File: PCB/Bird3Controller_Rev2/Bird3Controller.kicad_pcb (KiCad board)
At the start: 2 copper layers, 43 x 108 mm, 52 parts, among them IC1 M24C08-RMN6TP, J1 Bird 3 24-pin Connector, J2 TXW154028S0 Connector, J3 87832-2220, Q1 2N7002A, SW1 SW_Boot, SW2 SW_Reset, U1 ESP32-S3-WROOM-1, U3 SN65HVD231, U4 LMR36520ADDAR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

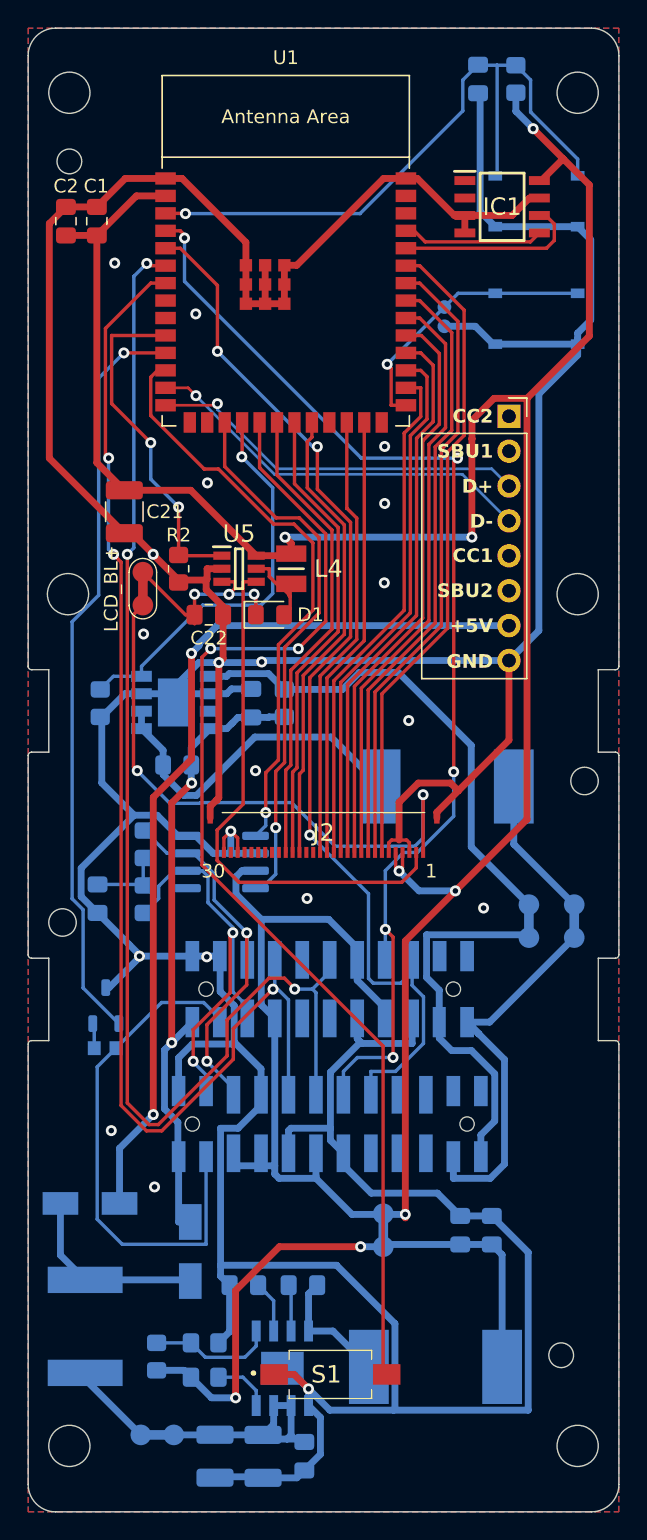
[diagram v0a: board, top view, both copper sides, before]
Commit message: Add more ground-plane vias
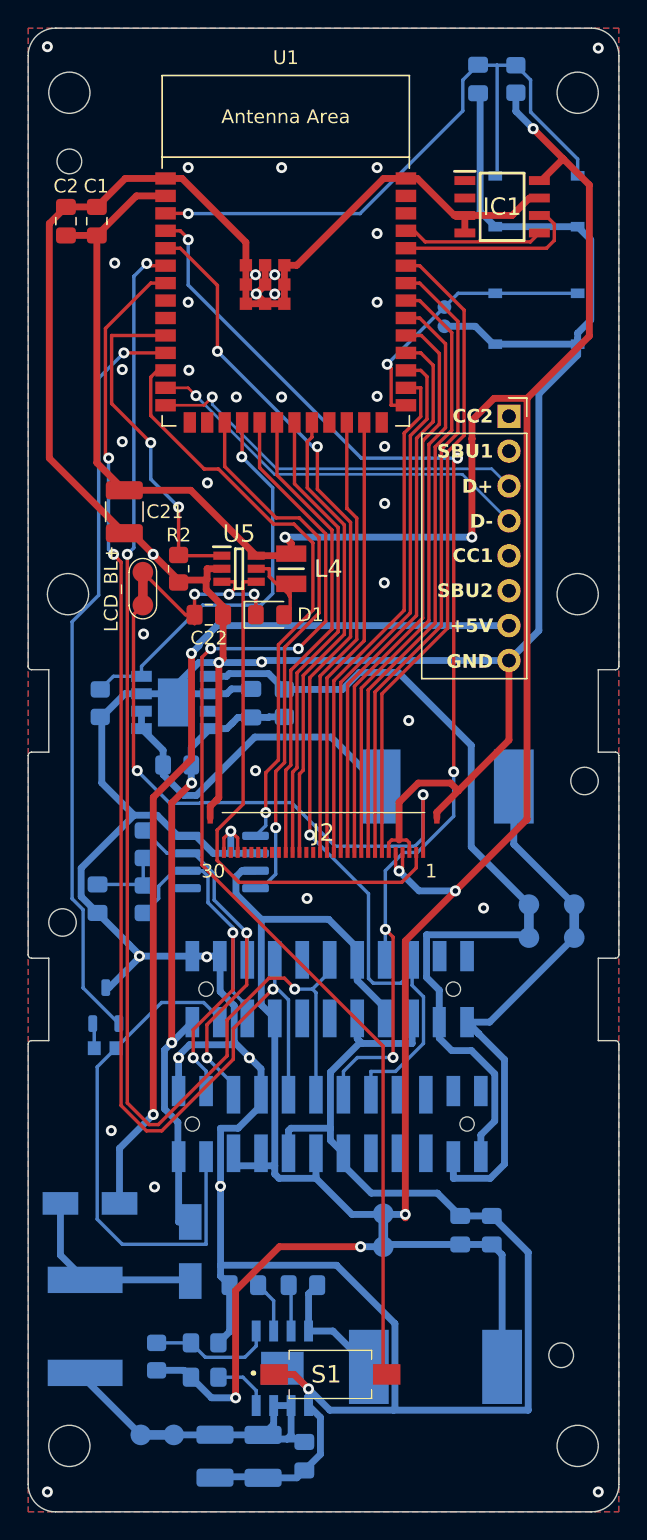
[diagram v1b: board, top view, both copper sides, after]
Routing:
- net GND: track 424.6 -> 425.3 mm, vias 20 -> 42

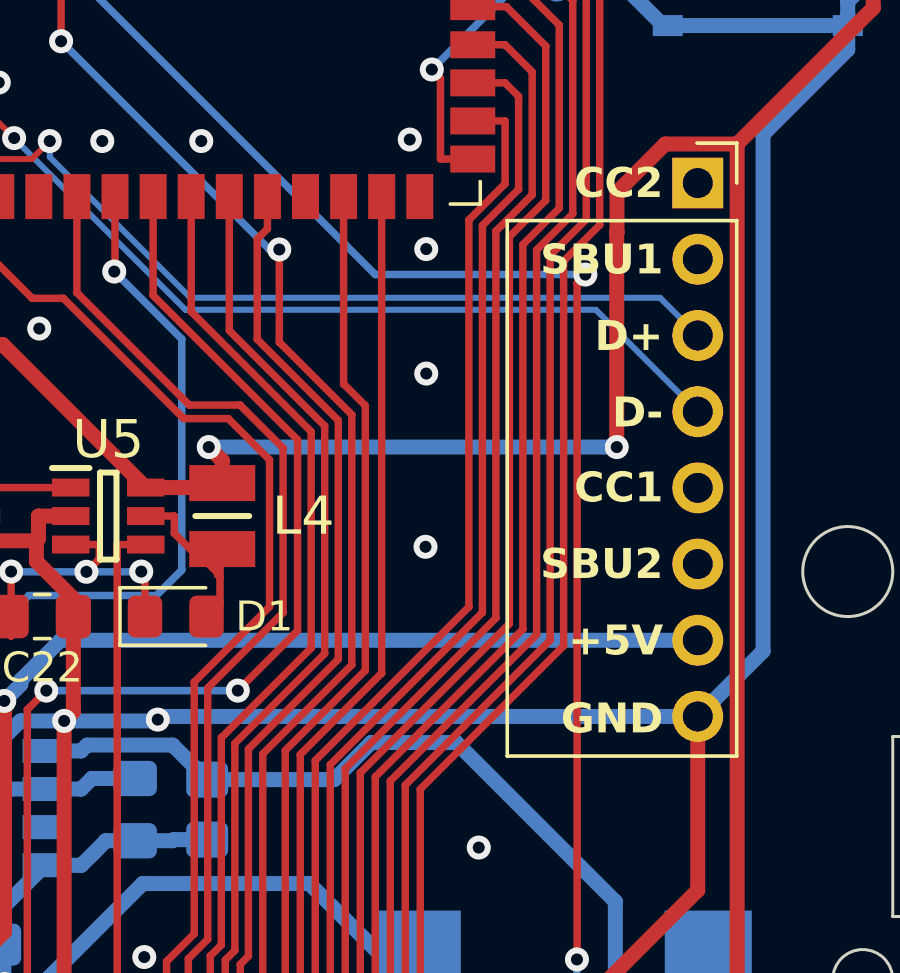
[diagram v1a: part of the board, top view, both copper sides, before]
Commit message: Push LCD data traces around and add more ground plane vias
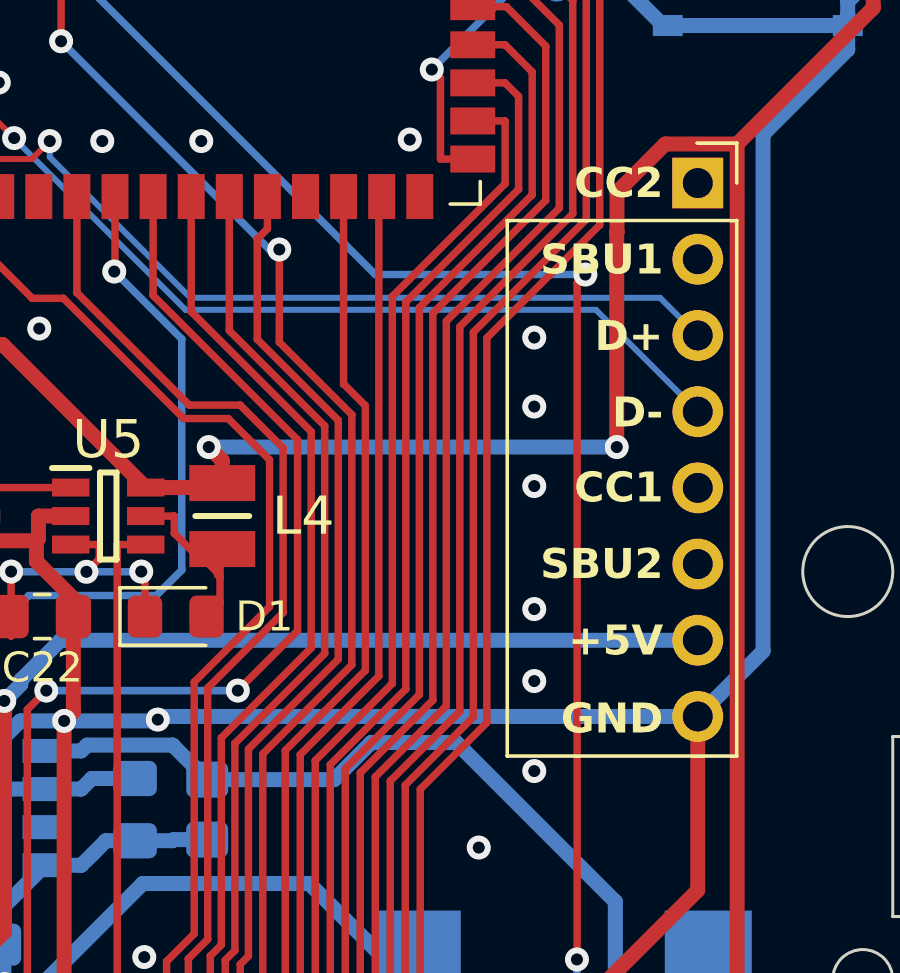
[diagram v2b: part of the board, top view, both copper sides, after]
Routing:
- net GND: vias 42 -> 45

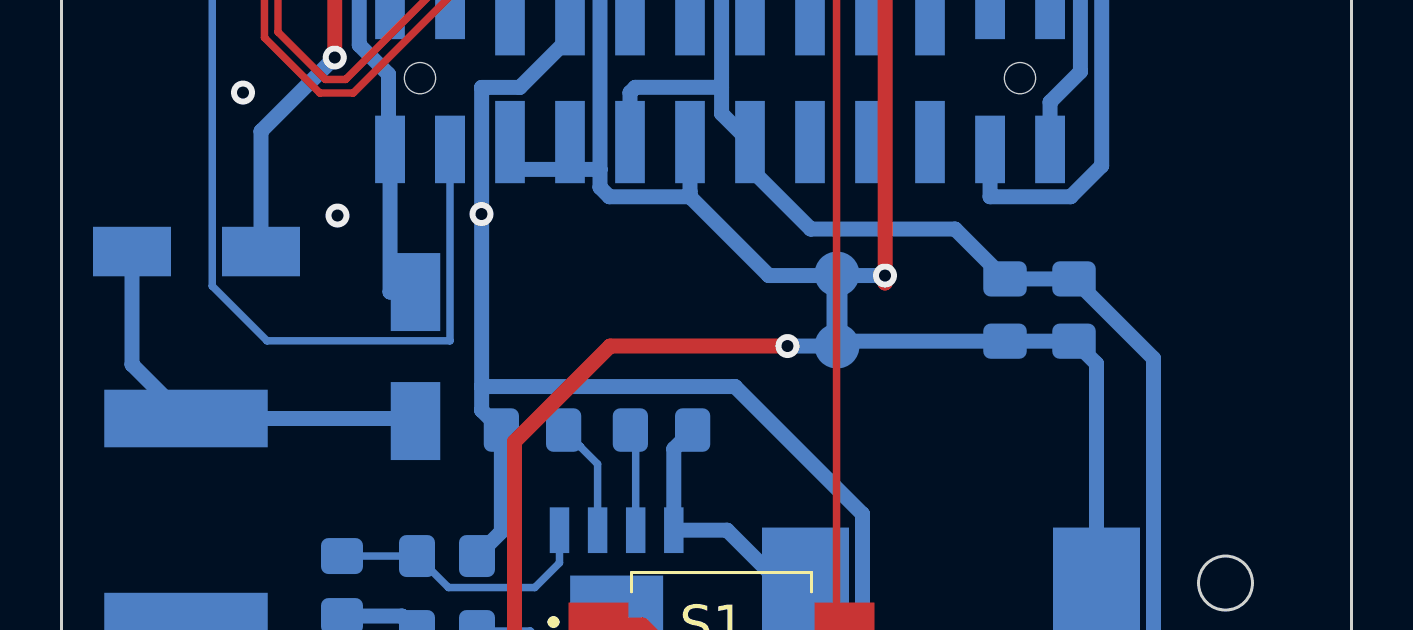
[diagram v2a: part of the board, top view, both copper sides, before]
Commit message: Add silkscreen reference to github repo and a placement for the JLCPCB order number
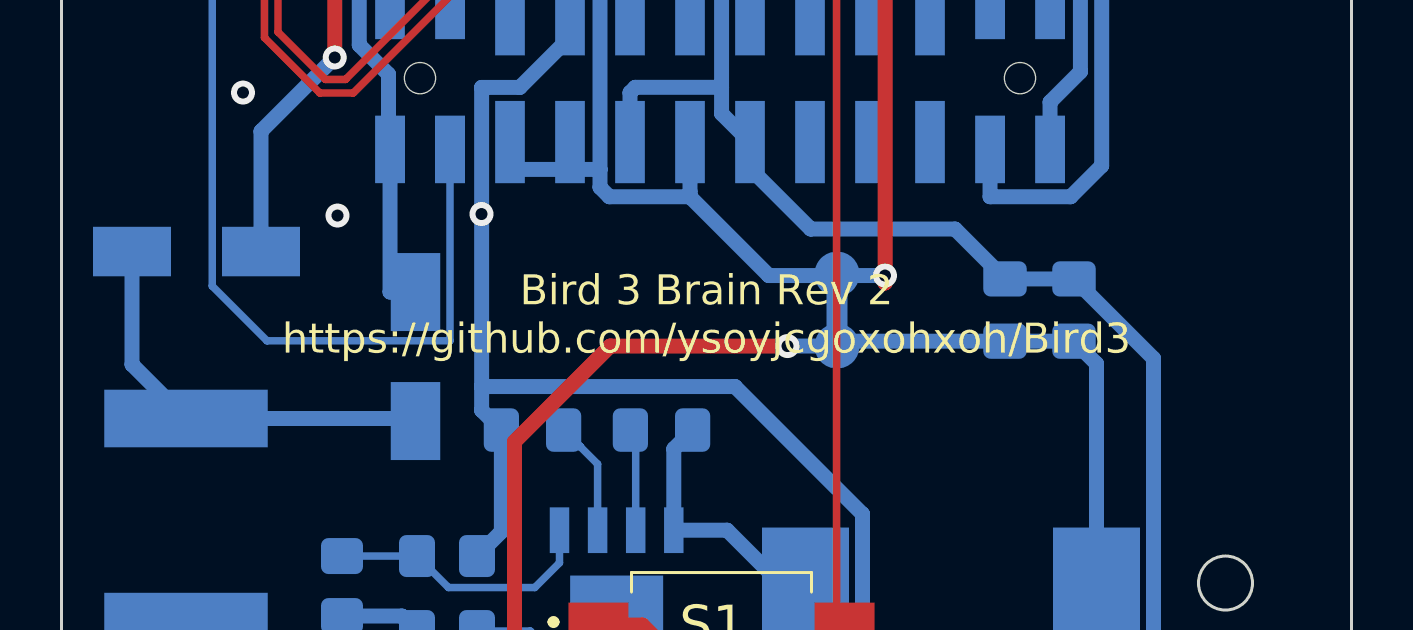
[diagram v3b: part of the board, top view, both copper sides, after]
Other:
- board text added: "Bird 3 Brain Rev 2 https://github.com/ysoyjcgoxohxoh/Bird3"
- board text added: "JLCJLCJLCJLC"
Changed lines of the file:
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@@
+		)
+	)
+	(gr_text "JLCJLCJLCJLC"
+		(at 190.05 135.1 -0)
+		(layer "B.SilkS")
+		(effects
+			(font
+				(size 1 1)
+				(thickness 0.15)
+			)
+			(justify mirror)
+		)
+	)
+	(gr_text "Bird 3 Brain Rev 2\nhttps://github.com/ysoyjcgoxohxoh/Bird3\n"
+		(at 182 129.65 0)
+		(layer "F.SilkS")
+		(effects
+			(font
+				(size 1 1)
+				(thickness 0.15)
+			)
 		)
 	)

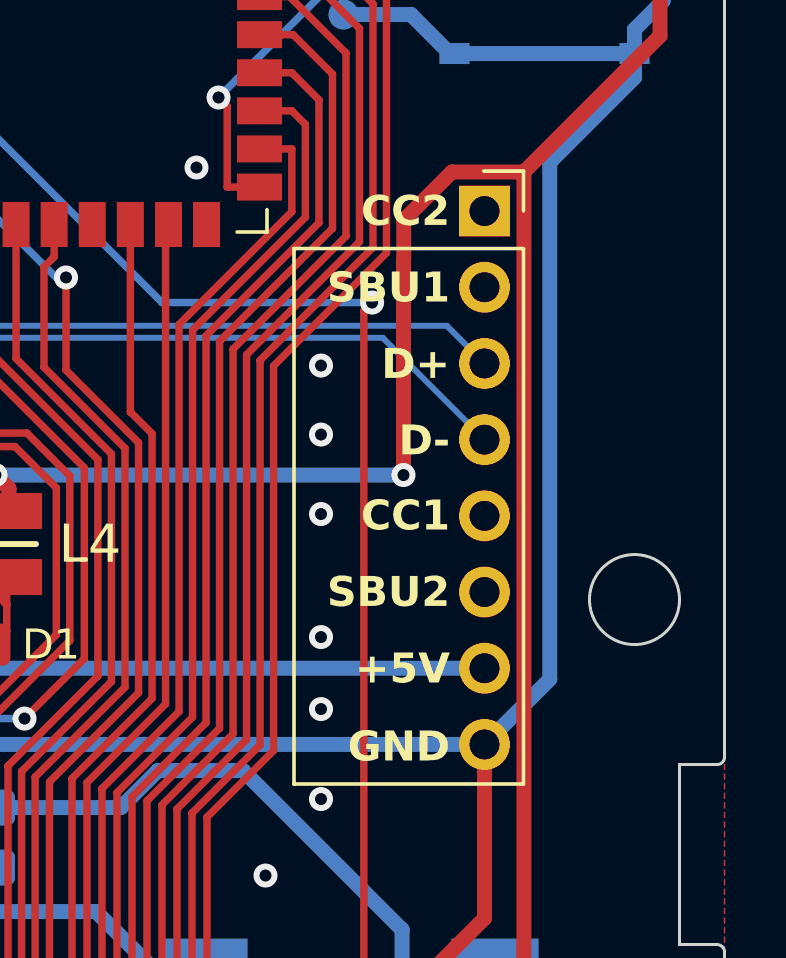
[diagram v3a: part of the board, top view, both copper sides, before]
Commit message: Update fields on PCB
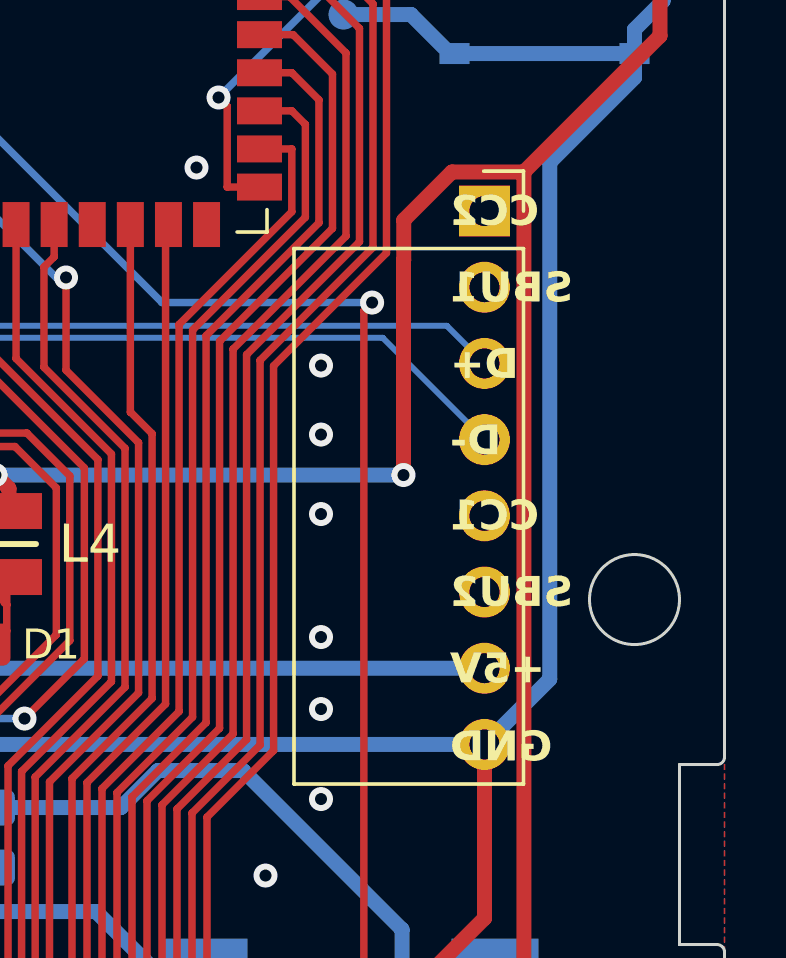
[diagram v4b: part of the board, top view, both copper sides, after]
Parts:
- C1, C3: value 0.1u -> 100n
